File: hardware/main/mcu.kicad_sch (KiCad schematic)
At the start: 8 parts, among them U1 Holyiot-18010-NRF52840

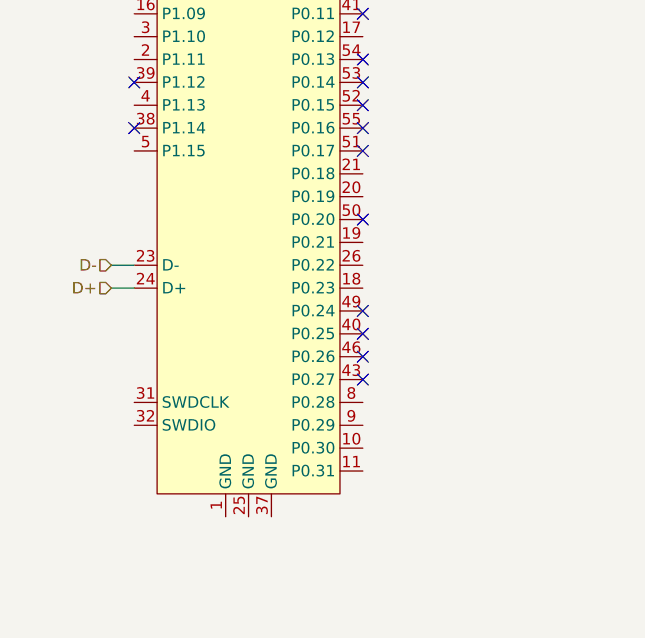
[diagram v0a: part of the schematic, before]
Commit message: Add programming/debug connection
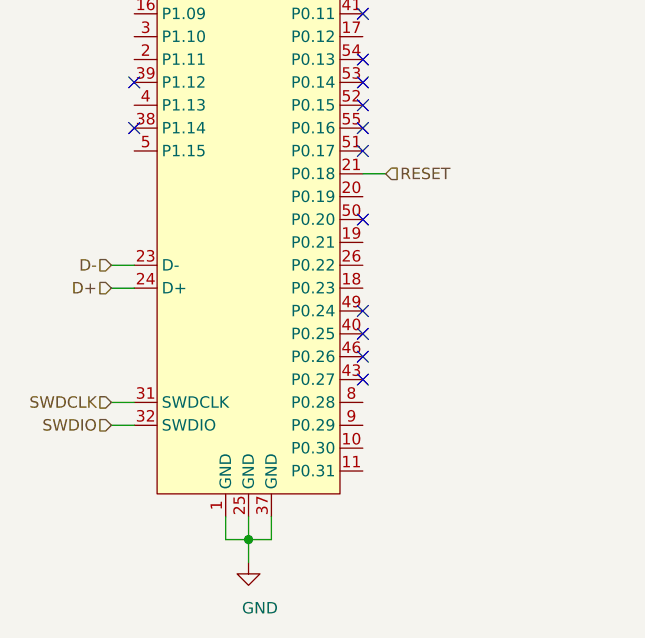
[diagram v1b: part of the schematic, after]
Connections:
- net GND: now also U1.1 (GND), U1.25 (GND), U1.37 (GND)
- net RESET: now reaches U1.21 (P0.18)
- net SWDCLK: now reaches U1.31 (SWDCLK)
- net SWDIO: now reaches U1.32 (SWDIO)
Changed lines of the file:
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@@
   (paper "A4")
   (junction (at 139.7 29.21) (diameter 1.016) (color 0 0 0 0))
+  (junction (at 139.7 130.81) (diameter 1.016) (color 0 0 0 0))
+  (no_connect (at 152.4 80.01))
+  (no_connect (at 152.4 59.69))
+  (no_connect (at 152.4 87.63))
+  (no_connect (at 127 80.01))
   (no_connect (at 152.4 110.49))
+  (no_connect (at 127 85.09))
   (no_connect (at 152.4 85.09))
-  (no_connect (at 152.4 87.63))
+  (no_connect (at 127 69.85))
   (no_connect (at 152.4 72.39))
+  (no_connect (at 152.4 82.55))
   (no_connect (at 152.4 77.47))
-  (no_connect (at 127 69.85))
-  (no_connect (at 152.4 107.95))
+  (no_connect (at 127 62.23))
   (no_connect (at 152.4 105.41))
   (no_connect (at 152.4 64.77))
-  (no_connect (at 152.4 59.69))
-  (no_connect (at 152.4 82.55))
-  (no_connect (at 127 62.23))
+  (no_connect (at 152.4 113.03))
   (no_connect (at 127 67.31))
-  (no_connect (at 127 80.01))
-  (no_connect (at 152.4 113.03))
   (no_connect (at 152.4 95.25))
-  (no_connect (at 152.4 80.01))
-  (no_connect (at 127 85.09))
+  (no_connect (at 152.4 107.95))
   (wire (pts (xy 116.84 29.21) (xy 139.7 29.21))
     (stroke (width 0) (type solid) (color 0 0 0 0))
@@
     (stroke (width 0) (type solid) (color 0 0 0 0))
   )
+  (wire (pts (xy 124.46 115.57) (xy 127 115.57))
+    (stroke (width 0) (type solid) (color 0 0 0 0))
+  )
+  (wire (pts (xy 124.46 118.11) (xy 127 118.11))
+    (stroke (width 0) (type solid) (color 0 0 0 0))
+  )
+  (wire (pts (xy 137.16 128.27) (xy 137.16 130.81))
+    (stroke (width 0) (type solid) (color 0 0 0 0))
+  )
+  (wire (pts (xy 137.16 130.81) (xy 139.7 130.81))
+    (stroke (width 0) (type solid) (color 0 0 0 0))
+  )
   (wire (pts (xy 139.7 29.21) (xy 139.7 25.4))
     (stroke (width 0) (type solid) (color 0 0 0 0))
   )
   (wire (pts (xy 139.7 44.45) (xy 139.7 29.21))
+    (stroke (width 0) (type solid) (color 0 0 0 0))
+  )
+  (wire (pts (xy 139.7 128.27) (xy 139.7 130.81))
+    (stroke (width 0) (type solid) (color 0 0 0 0))
+  )
+  (wire (pts (xy 139.7 130.81) (xy 139.7 133.35))
+    (stroke (width 0) (type solid) (color 0 0 0 0))
+  )
+  (wire (pts (xy 139.7 130.81) (xy 142.24 130.81))
+    (stroke (width 0) (type solid) (color 0 0 0 0))
+  )
+  (wire (pts (xy 142.24 130.81) (xy 142.24 128.27))
+    (stroke (width 0) (type solid) (color 0 0 0 0))
+  )
+  (wire (pts (xy 152.4 90.17) (xy 154.94 90.17))
     (stroke (width 0) (type solid) (color 0 0 0 0))
   )
@@
     (effects (font (size 1.27 1.27)) (justify right))
   )
+  (hierarchical_label "SWDCLK" (shape input) (at 124.46 115.57 180)
+    (effects (font (size 1.27 1.27)) (justify right))
+  )
+  (hierarchical_label "SWDIO" (shape input) (at 124.46 118.11 180)
+    (effects (font (size 1.27 1.27)) (justify right))
+  )
   (hierarchical_label "VCC_SW" (shape input) (at 139.7 25.4 90)
+    (effects (font (size 1.27 1.27)) (justify left))
+  )
+  (hierarchical_label "RESET" (shape input) (at 154.94 90.17 0)
     (effects (font (size 1.27 1.27)) (justify left))
   )
@@
       (effects (font (size 1.27 1.27)) hide)
     )
+  )
+  (symbol (lib_id "power:GND") (at 139.7 133.35 0) (unit 1)
+    (in_bom yes) (on_board yes)
+    (property "Reference" "#PWR?" (id 0) (at 139.7 139.7 0)
+      (effects (font (size 1.27 1.27)) hide)
+    )
+    (property "Value" "GND" (id 1) (at 140.97 138.43 0))
+    (property "Footprint" "" (id 2) (at 139.7 133.35 0)
+      (effects (font (size 1.27 1.27)) hide)
+    )
+    (property "Datasheet" "" (id 3) (at 139.7 133.35 0)
+      (effects (font (size 1.27 1.27)) hide)
+    )

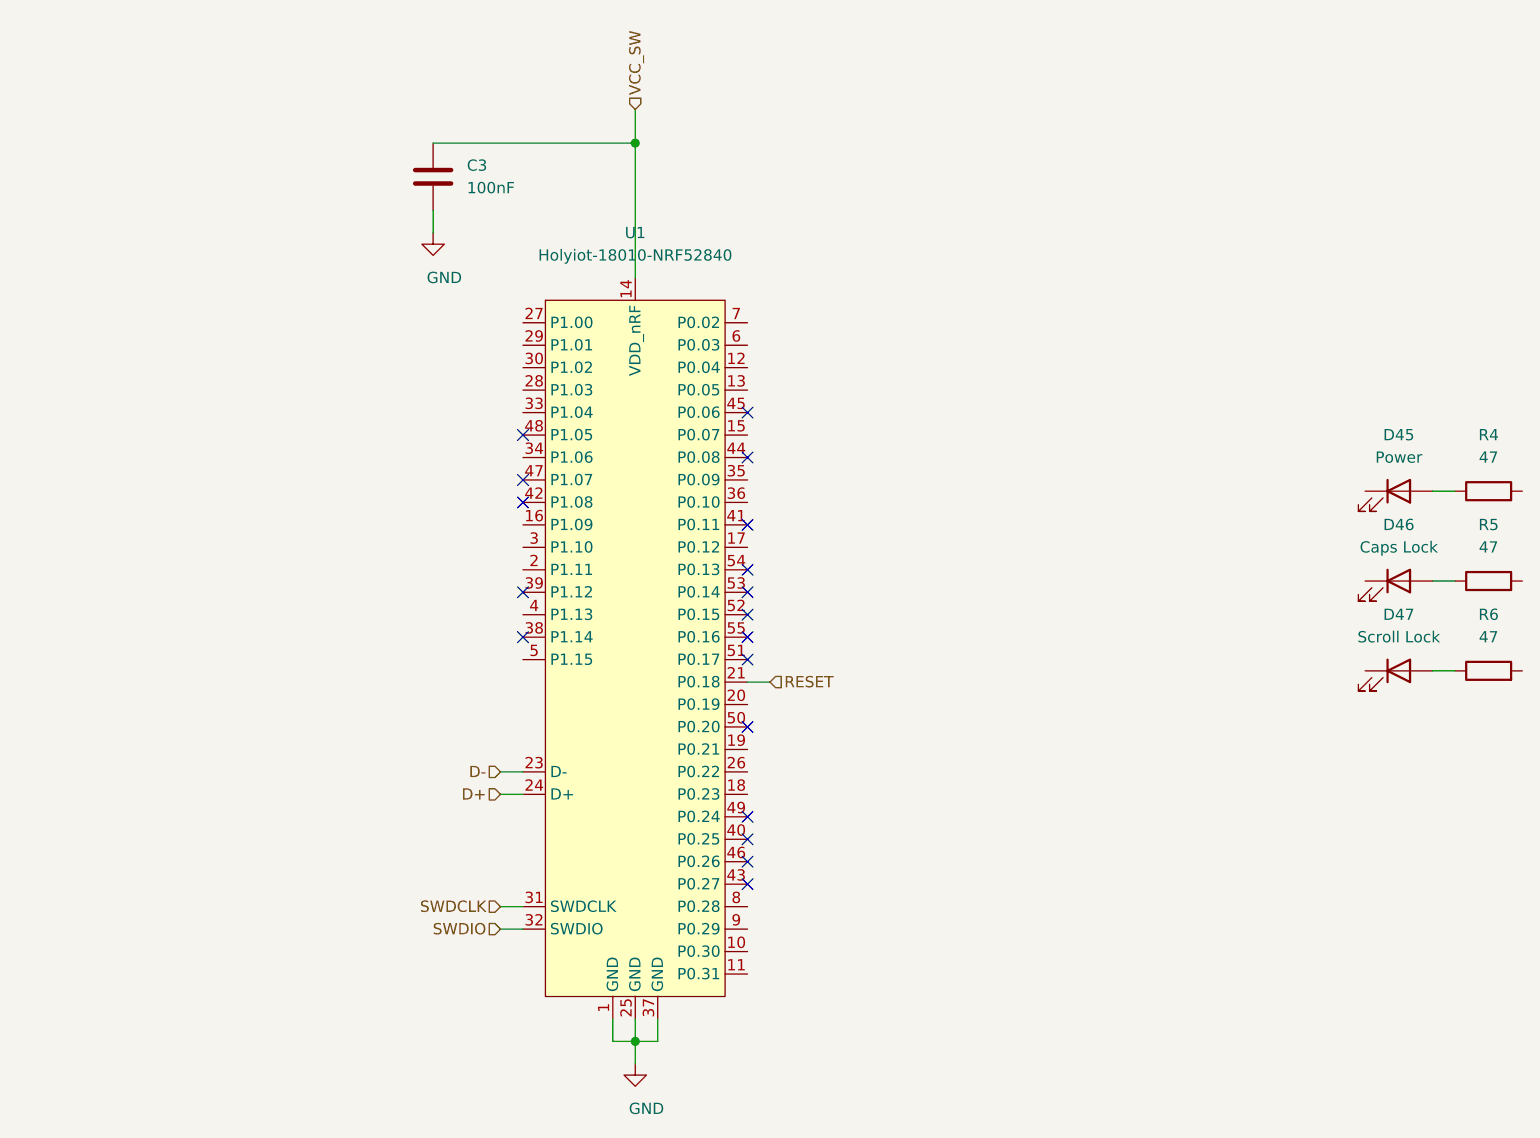
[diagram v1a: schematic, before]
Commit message: Add connections to the NRF module
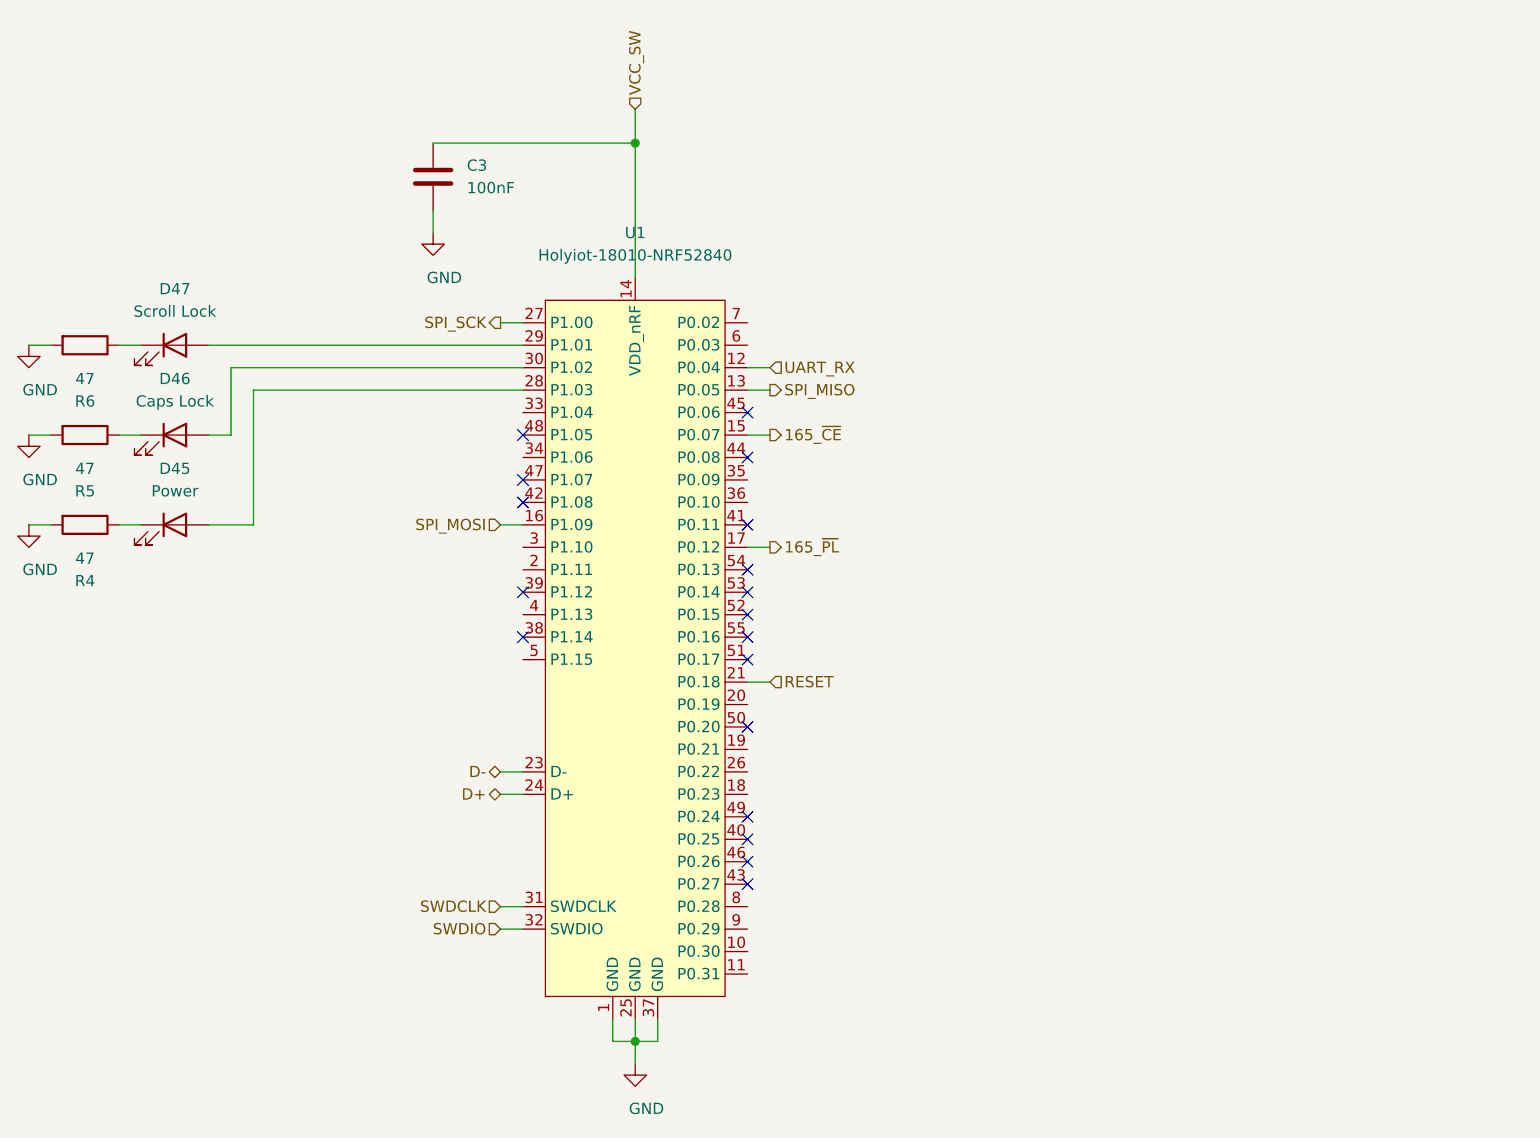
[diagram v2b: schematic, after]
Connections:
- net GND: now also R4.2, R5.2, R6.2
- net at D47.1 (K): now also R6.1
- net at D47.2 (A): now also U1.29 (P1.01); no longer R6.1
- net at D45.1 (K): now also R4.1
- net at D45.2 (A): now also U1.28 (P1.03); no longer R4.1
- net UART_RX: now reaches U1.12 (P0.04)
- net SPI_MISO: now reaches U1.13 (P0.05)
- net 165_~CE: now reaches U1.15 (P0.07)
- net SPI_MOSI: now reaches U1.16 (P1.09)
- net 165_~PL: now reaches U1.17 (P0.12)
- net SPI_SCK: now reaches U1.27 (P1.00)
- net at U1.30 (P1.02): now also D46.2 (A)
- net at R5.1: now also D46.1 (K); no longer D46.2 (A)
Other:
- moved on the sheet: D45, D46, D47, R4, R5, R6

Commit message: Add footprints to many symbols
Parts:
- C3: footprint (none) -> Capacitor_SMD:C_0201_0603Metric_Pad0.64x0.40mm_HandSolder; Mouser (none) -> 581-06033C104KAT4A; Part Name (none) -> 06033C104KAT4A
- D45, D46, D47: footprint (none) -> Diode_SMD:D_0603_1608Metric_Pad1.05x0.95mm_HandSolder; Mouser (none) -> 710-150060SS75000; Part Name (none) -> 150060SS75000
- R4, R5, R6: footprint (none) -> Resistor_SMD:R_0603_1608Metric_Pad0.98x0.95mm_HandSolder
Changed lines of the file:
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@@
   (junction (at 139.7 29.21) (diameter 1.016) (color 0 0 0 0))
   (junction (at 139.7 130.81) (diameter 1.016) (color 0 0 0 0))
-  (no_connect (at 152.4 80.01))
-  (no_connect (at 152.4 59.69))
-  (no_connect (at 152.4 87.63))
-  (no_connect (at 127 80.01))
-  (no_connect (at 152.4 110.49))
-  (no_connect (at 127 85.09))
+  (no_connect (at 152.4 64.77))
   (no_connect (at 152.4 85.09))
   (no_connect (at 127 69.85))
+  (no_connect (at 127 62.23))
+  (no_connect (at 152.4 59.69))
+  (no_connect (at 152.4 107.95))
+  (no_connect (at 152.4 105.41))
+  (no_connect (at 127 85.09))
   (no_connect (at 152.4 72.39))
+  (no_connect (at 152.4 113.03))
+  (no_connect (at 152.4 95.25))
+  (no_connect (at 127 80.01))
+  (no_connect (at 152.4 80.01))
+  (no_connect (at 152.4 87.63))
+  (no_connect (at 127 67.31))
+  (no_connect (at 152.4 77.47))
+  (no_connect (at 152.4 110.49))
   (no_connect (at 152.4 82.55))
-  (no_connect (at 152.4 77.47))
-  (no_connect (at 127 62.23))
-  (no_connect (at 152.4 105.41))
-  (no_connect (at 152.4 64.77))
-  (no_connect (at 152.4 113.03))
-  (no_connect (at 127 67.31))
-  (no_connect (at 152.4 95.25))
-  (no_connect (at 152.4 107.95))
   (wire (pts (xy 71.12 52.07) (xy 73.66 52.07))
     (stroke (width 0) (type solid) (color 0 0 0 0))
@@
     (property "Reference" "R6" (id 0) (at 77.47 58.42 90))
     (property "Value" "47" (id 1) (at 77.47 55.88 90))
-    (property "Footprint" "" (id 2) (at 77.47 50.292 90)
+    (property "Footprint" "Resistor_SMD:R_0603_1608Metric_Pad0.98x0.95mm_HandSolder" (id 2) (at 77.47 50.292 90)
       (effects (font (size 1.27 1.27)) hide)
     )
@@
     (property "Reference" "R5" (id 0) (at 77.47 68.58 90))
     (property "Value" "47" (id 1) (at 77.47 66.04 90))
-    (property "Footprint" "" (id 2) (at 77.47 60.452 90)
+    (property "Footprint" "Resistor_SMD:R_0603_1608Metric_Pad0.98x0.95mm_HandSolder" (id 2) (at 77.47 60.452 90)
       (effects (font (size 1.27 1.27)) hide)
     )
@@
     (property "Reference" "R4" (id 0) (at 77.47 78.74 90))
     (property "Value" "47" (id 1) (at 77.47 76.2 90))
-    (property "Footprint" "" (id 2) (at 77.47 70.612 90)
+    (property "Footprint" "Resistor_SMD:R_0603_1608Metric_Pad0.98x0.95mm_HandSolder" (id 2) (at 77.47 70.612 90)
       (effects (font (size 1.27 1.27)) hide)
     )
@@
     (property "Reference" "D47" (id 0) (at 87.63 45.72 0))
     (property "Value" "Scroll Lock" (id 1) (at 87.63 48.26 0))
-    (property "Footprint" "" (id 2) (at 87.63 52.07 0)
-      (effects (font (size 1.27 1.27)) hide)
-    )
-    (property "Datasheet" "~" (id 3) (at 87.63 52.07 0)
+    (property "Footprint" "Diode_SMD:D_0603_1608Metric_Pad1.05x0.95mm_HandSolder" (id 2) (at 87.63 52.07 0)
+      (effects (font (size 1.27 1.27)) hide)
+    )
+    (property "Datasheet" "https://www.mouser.de/datasheet/2/445/150060SS75000-1715253.pdf" (id 3) (at 87.63 52.07 0)
+      (effects (font (size 1.27 1.27)) hide)
+    )
+    (property "Mouser" "710-150060SS75000" (id 4) (at 87.63 52.07 0)
+      (effects (font (size 1.27 1.27)) hide)
+    )
+    (property "Part Name" "150060SS75000 " (id 5) (at 87.63 52.07 0)
       (effects (font (size 1.27 1.27)) hide)
     )
@@
     (property "Reference" "D46" (id 0) (at 87.63 55.88 0))
     (property "Value" "Caps Lock" (id 1) (at 87.63 58.42 0))
-    (property "Footprint" "" (id 2) (at 87.63 62.23 0)
-      (effects (font (size 1.27 1.27)) hide)
-    )
-    (property "Datasheet" "~" (id 3) (at 87.63 62.23 0)
+    (property "Footprint" "Diode_SMD:D_0603_1608Metric_Pad1.05x0.95mm_HandSolder" (id 2) (at 87.63 62.23 0)
+      (effects (font (size 1.27 1.27)) hide)
+    )
+    (property "Datasheet" "https://www.mouser.de/datasheet/2/445/150060SS75000-1715253.pdf" (id 3) (at 87.63 62.23 0)
+      (effects (font (size 1.27 1.27)) hide)
+    )
+    (property "Mouser" "710-150060SS75000" (id 4) (at 87.63 62.23 0)
+      (effects (font (size 1.27 1.27)) hide)
+    )
+    (property "Part Name" "150060SS75000 " (id 5) (at 87.63 62.23 0)
       (effects (font (size 1.27 1.27)) hide)
     )
@@
     (property "Reference" "D45" (id 0) (at 87.63 66.04 0))
     (property "Value" "Power" (id 1) (at 87.63 68.58 0))
-    (property "Footprint" "" (id 2) (at 87.63 72.39 0)
-      (effects (font (size 1.27 1.27)) hide)
-    )
-    (property "Datasheet" "~" (id 3) (at 87.63 72.39 0)
+    (property "Footprint" "Diode_SMD:D_0603_1608Metric_Pad1.05x0.95mm_HandSolder" (id 2) (at 87.63 72.39 0)
+      (effects (font (size 1.27 1.27)) hide)
+    )
+    (property "Datasheet" "https://www.mouser.de/datasheet/2/445/150060SS75000-1715253.pdf" (id 3) (at 87.63 72.39 0)
+      (effects (font (size 1.27 1.27)) hide)
+    )
+    (property "Mouser" "710-150060SS75000" (id 4) (at 87.63 72.39 0)
+      (effects (font (size 1.27 1.27)) hide)
+    )
+    (property "Part Name" "150060SS75000 " (id 5) (at 87.63 72.39 0)
       (effects (font (size 1.27 1.27)) hide)
     )
@@
       (effects (font (size 1.27 1.27)) (justify left))
     )
-    (property "Footprint" "" (id 2) (at 117.8052 36.83 0)
-      (effects (font (size 1.27 1.27)) hide)
-    )
-    (property "Datasheet" "~" (id 3) (at 116.84 33.02 0)
-      (effects (font (size 1.27 1.27)) hide)
-    )
+    (property "Footprint" "Capacitor_SMD:C_0201_0603Metric_Pad0.64x0.40mm_HandSolder" (id 2) (at 117.8052 36.83 0)
+      (effects (font (size 1.27 1.27)) hide)
+    )
+    (property "Datasheet" "https://www.mouser.de/datasheet/2/40/X7RDielectric-777024.pdf" (id 3) (at 116.84 33.02 0)
+      (effects (font (size 1.27 1.27)) hide)
+    )
+    (property "Mouser" "581-06033C104KAT4A" (id 4) (at 116.84 33.02 0)
+      (effects (font (size 1.27 1.27)) hide)
+    )
+    (property "Part Name" "06033C104KAT4A " (id 5) (at 116.84 33.02 0)
+      (effects (font (size 1.27 1.27)) hide)
+    )
